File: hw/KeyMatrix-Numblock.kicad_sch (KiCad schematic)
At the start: 62 parts, among them SW2300 SW_Cherry_MX_RGB, SW2301 SW_Cherry_MX_RGB, SW2302 SW_Cherry_MX_RGB, SW2303 SW_Cherry_MX_RGB, SW2304 SW_Cherry_MX_RGB, SW2305 SW_Cherry_MX_RGB, SW2306 SW_Cherry_MX_RGB, SW2307 SW_Cherry_MX_RGB, SW2308 SW_Cherry_MX_RGB, SW2309 SW_Cherry_MX_RGB, SW2310 SW_Cherry_MX_RGB, SW2311 SW_Cherry_MX_RGB, SW2312 SW_Cherry_MX_RGB, SW2313 SW_Cherry_MX_RGB, SW2314 SW_Cherry_MX_RGB, SW2315 SW_Cherry_MX_RGB, SW2316 SW_Cherry_MX_RGB, SW2317 SW_Cherry_MX_RGB, X2300 STAB-0G990224, X2301 STAB-0G990224, X2302 STAB-0G990224, X2303 Keycap-R1-1x1, X2304 Keycap-R1-1x1, X2305 Keycap-R1-1x1, X2306 Keycap-R1-1x1, X2307 Keycap-R1-1x1, X2308 Keycap-R1-1x1, X2309 Keycap-R1-1x1, X2310 Keycap-R1-1x1, X2311 Keycap-R1-2x1, X2312 Keycap-R1-1x1, X2313 Keycap-R1-1x1, X2314 Keycap-R1-1x1, X2315 Keycap-R1-1x1, X2316 Keycap-R1-1x1, X2317 Keycap-R1-1x1, X2318 Keycap-R1-2x1, X2319 Keycap-R1-2x1, X2320 Keycap-R1-1x1

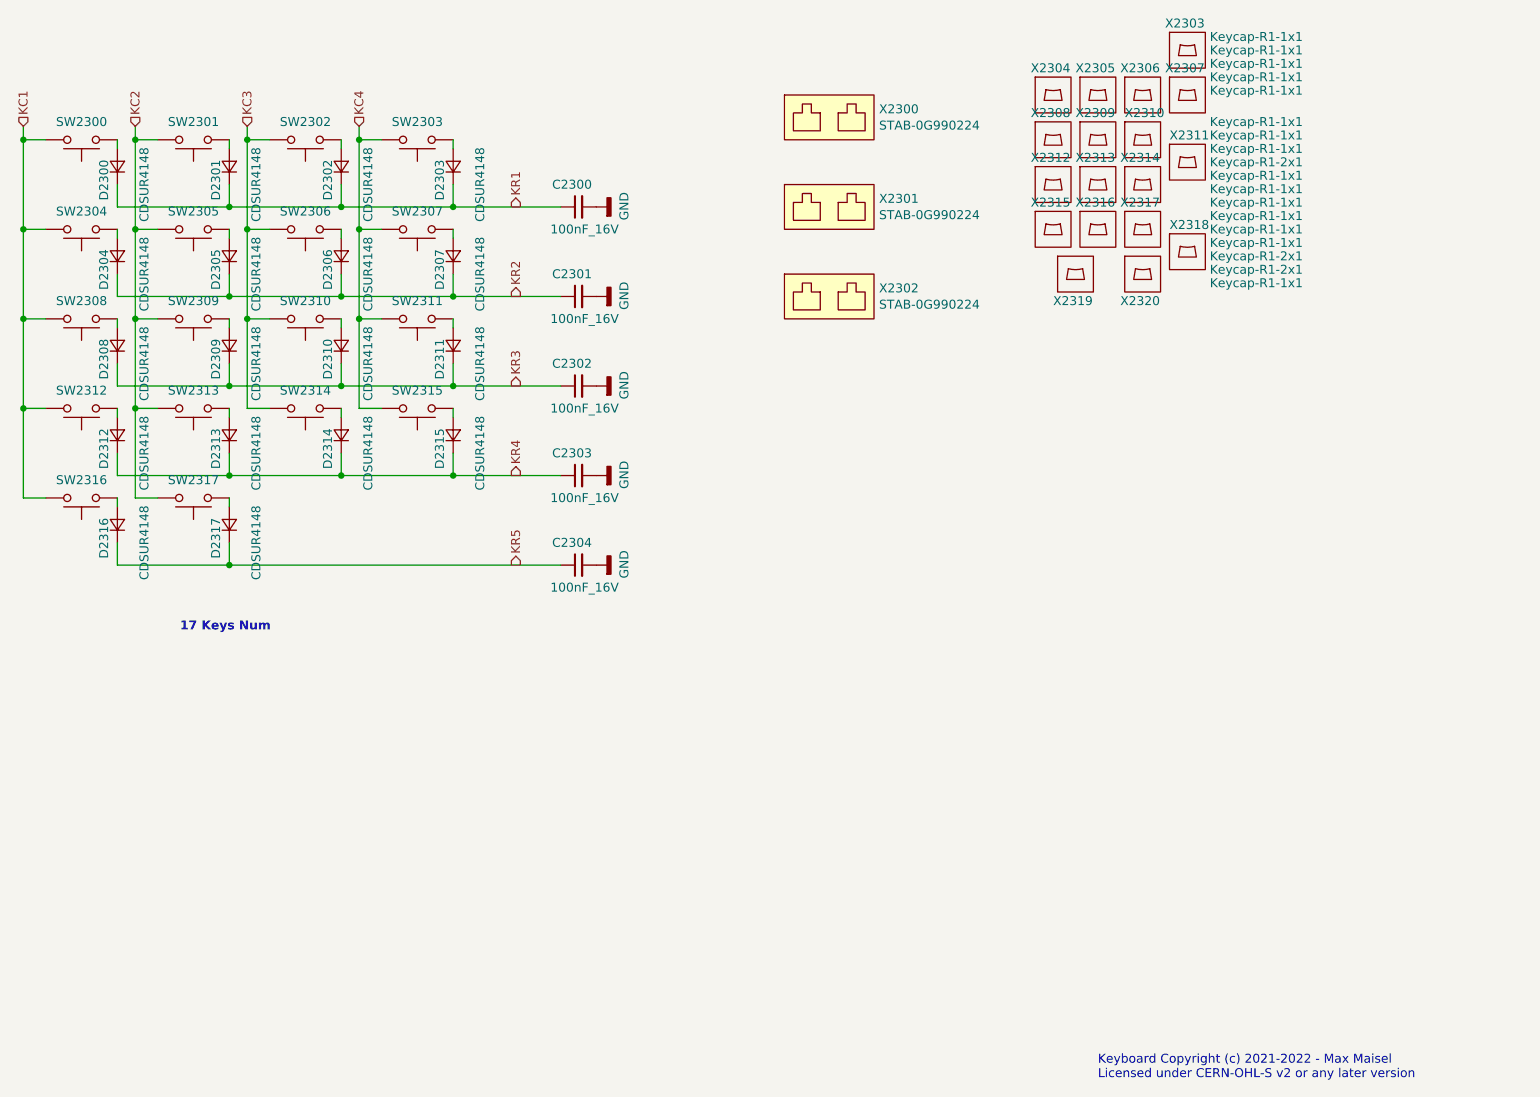
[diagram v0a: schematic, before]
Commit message: Add ESD diodes to key matrix pins.
Better save than sorry.
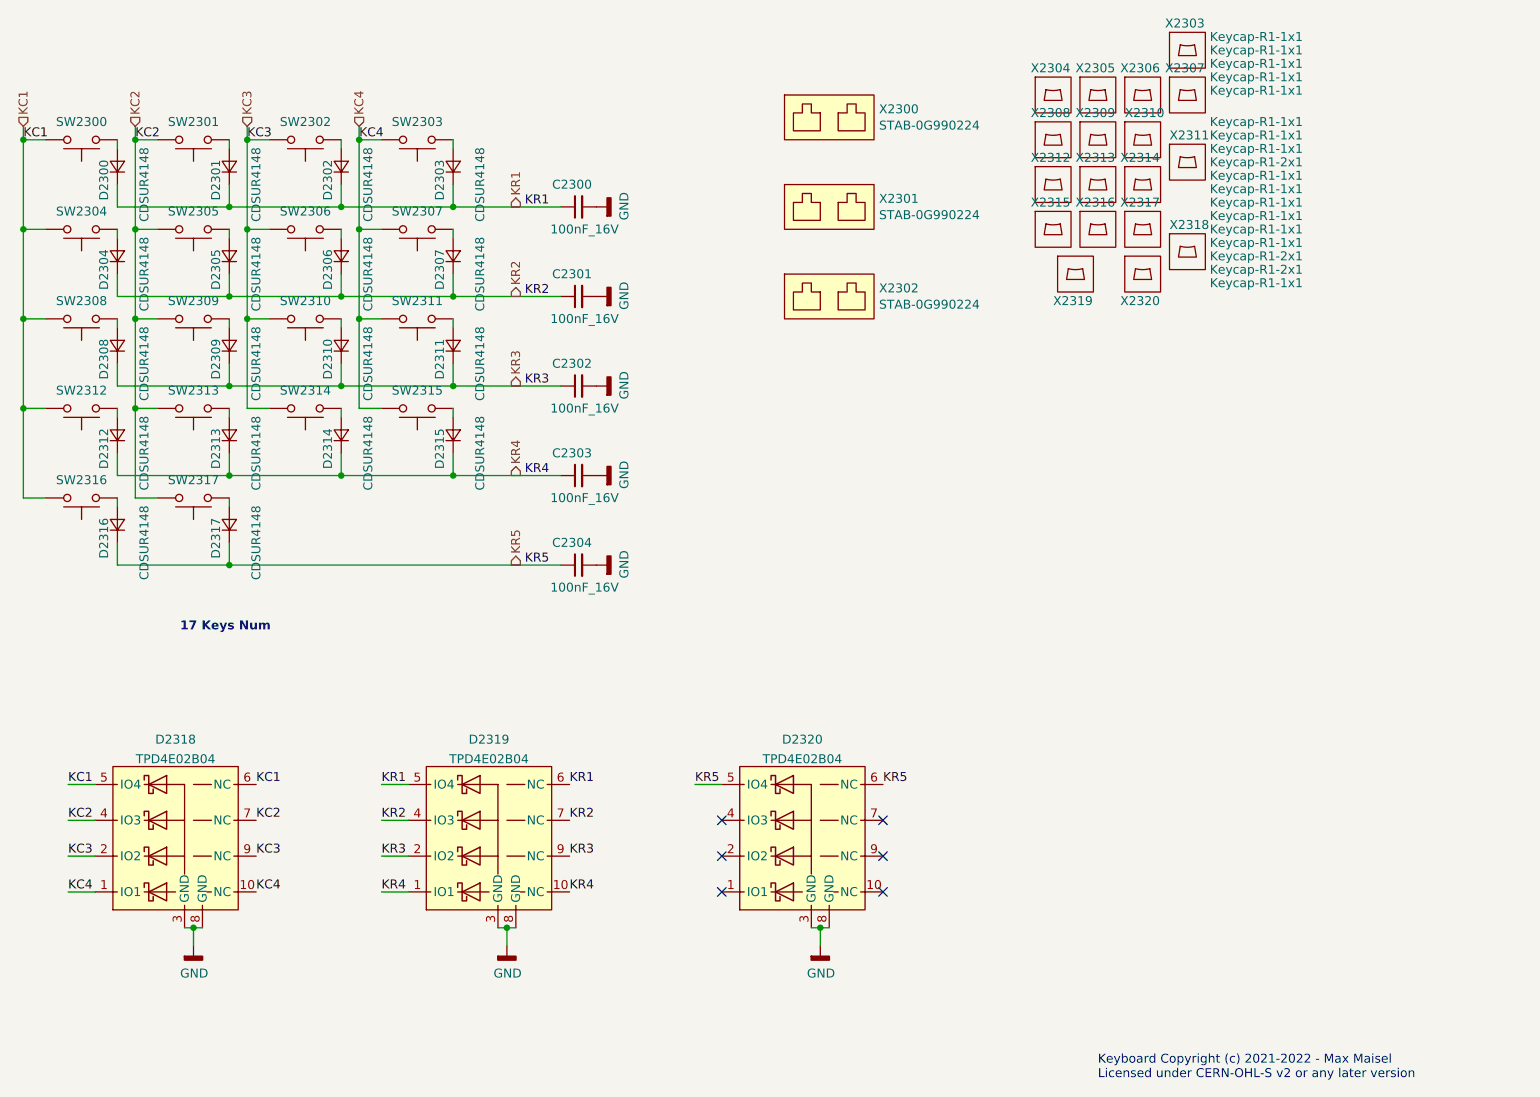
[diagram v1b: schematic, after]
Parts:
- added D2318, D2319, D2320: TPD4E02B04, Keyboard:USON10, symbol Keyboard:TPD4E02B04
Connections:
- net GND: now also D2318.3 (GND), D2318.8 (GND), D2319.3 (GND), D2319.8 (GND), D2320.3 (GND), D2320.8 (GND)
- net KC1: now also D2318.5 (IO4), D2318.6 (NC)
- net KC2: now also D2318.4 (IO3), D2318.7 (NC)
- net KC3: now also D2318.2 (IO2), D2318.9 (NC)
- net KC4: now also D2318.1 (IO1), D2318.10 (NC)
- net KR1: now also D2319.5 (IO4), D2319.6 (NC)
- net KR2: now also D2319.4 (IO3), D2319.7 (NC)
- net KR3: now also D2319.2 (IO2), D2319.9 (NC)
- net KR4: now also D2319.1 (IO1), D2319.10 (NC)
- net KR5: now also D2320.5 (IO4), D2320.6 (NC)
- no-connect marks 0 -> 6

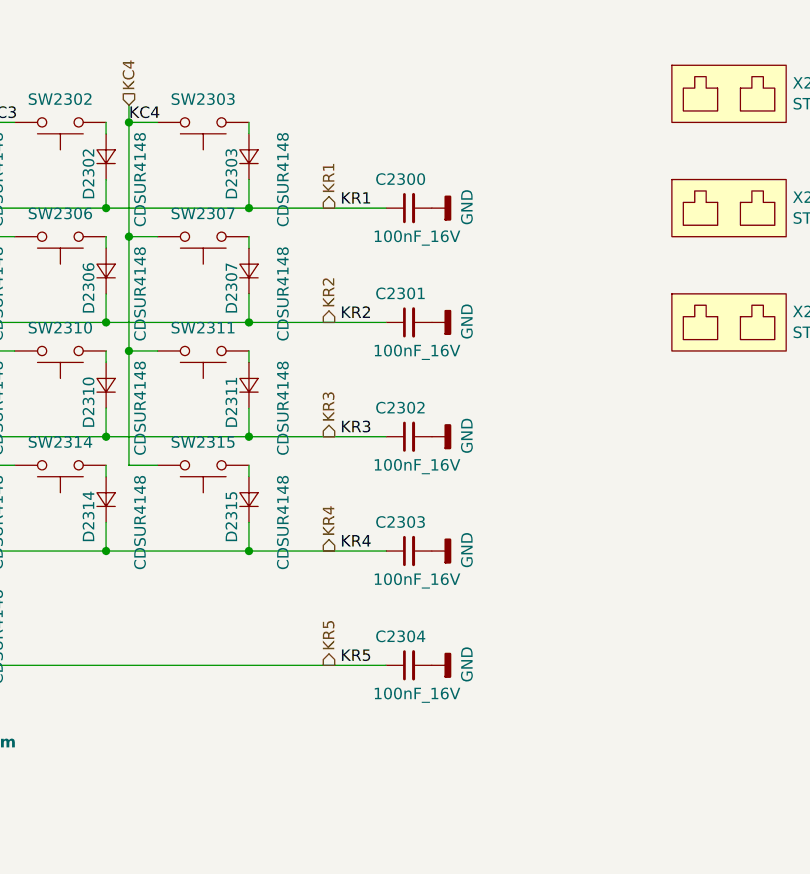
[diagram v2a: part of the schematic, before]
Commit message: Change key matrix capacitors to 220pF.
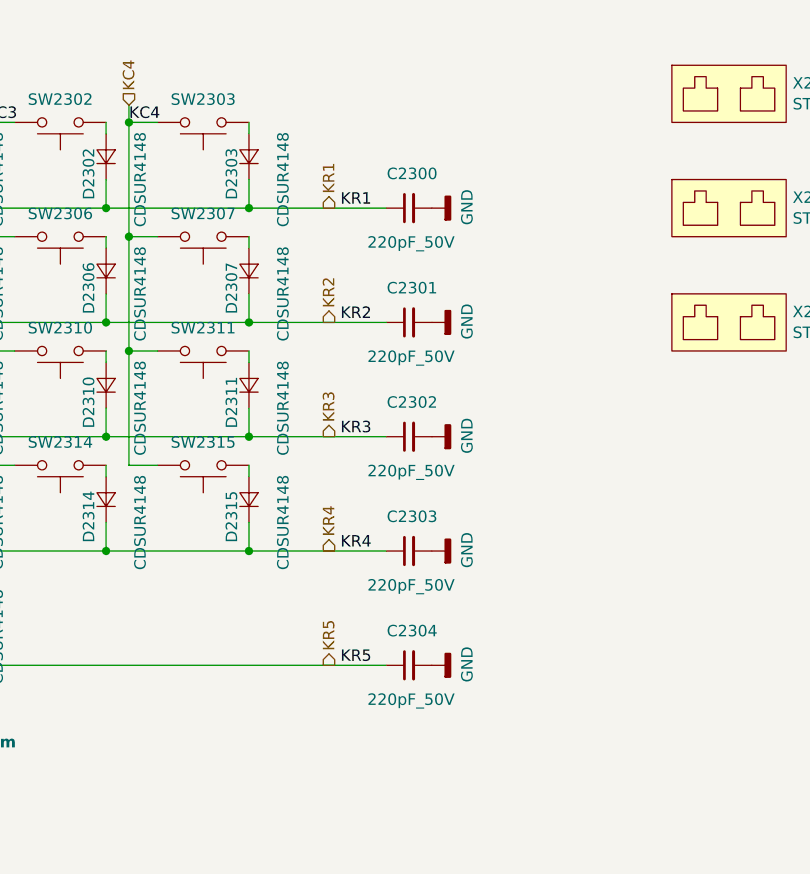
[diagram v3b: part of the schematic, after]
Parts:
- removed C2300, C2301, C2302, C2303, C2304: 100nF_16V, Keyboard:C_0402, symbol Keyboard:100nF_16V
- added C2300, C2301, C2302, C2303, C2304: 220pF_50V, Keyboard:C_0402, symbol Keyboard:220pF_50V
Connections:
- net GND: now also C2300.2, C2301.2, C2302.2, C2303.2, C2304.2
- net KR1: now also C2300.1
- net KR2: now also C2301.1
- net KR3: now also C2302.1
- net KR4: now also C2303.1
- net KR5: now also C2304.1
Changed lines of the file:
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@@
-    (pin "2")
-  )
-  (symbol (lib_id "Keyboard:100nF_16V") (at 104.14 47.625 90) (unit 1)
-    (in_bom yes) (on_board yes)
-    (property "Reference" "C2300" (id 0) (at 106.045 44.45 90)
-      (effects (font (size 1.27 1.27)) (justify left))
-    )
-    (property "Value" "100nF_16V" (id 1) (at 109.855 50.8 90)
-      (effects (font (size 1.27 1.27)) (justify left))
-    )
-    (property "Footprint" "Keyboard:C_0402" (id 2) (at 104.902 49.911 0)
-      (effects (font (size 1.27 1.27)) hide)
-    )
-    (property "Datasheet" "80-C0402C104K4R" (id 3) (at 102.362 47.371 0)
-      (effects (font (size 1.27 1.27)) hide)
-    )
-    (property "mouser#" "80-C0402C104K4R" (id 4) (at 99.822 44.831 0)
-      (effects (font (size 1.524 1.524)) hide)
-    )
-    (pin "1")
     (pin "2")
   )
@@
     (pin "1")
   )
-  (symbol (lib_id "Keyboard:100nF_16V") (at 104.14 73.025 90) (unit 1)
-    (in_bom yes) (on_board yes)
-    (property "Reference" "C2302" (id 0) (at 106.045 69.85 90)
-      (effects (font (size 1.27 1.27)) (justify left))
-    )
-    (property "Value" "100nF_16V" (id 1) (at 109.855 76.2 90)
-      (effects (font (size 1.27 1.27)) (justify left))
-    )
-    (property "Footprint" "Keyboard:C_0402" (id 2) (at 104.902 75.311 0)
-      (effects (font (size 1.27 1.27)) hide)
-    )
-    (property "Datasheet" "80-C0402C104K4R" (id 3) (at 102.362 72.771 0)
-      (effects (font (size 1.27 1.27)) hide)
-    )
-    (property "mouser#" "80-C0402C104K4R" (id 4) (at 99.822 70.231 0)
-      (effects (font (size 1.524 1.524)) hide)
-    )
-    (pin "1")
-    (pin "2")
-  )
   (symbol (lib_id "Keyboard:GND") (at 106.68 73.025 90) (unit 1)
     (in_bom yes) (on_board yes)
@@
     (pin "1")
   )
-  (symbol (lib_id "Keyboard:100nF_16V") (at 104.14 85.725 90) (unit 1)
-    (in_bom yes) (on_board yes)
-    (property "Reference" "C2303" (id 0) (at 106.045 82.55 90)
-      (effects (font (size 1.27 1.27)) (justify left))
-    )
-    (property "Value" "100nF_16V" (id 1) (at 109.855 88.9 90)
-      (effects (font (size 1.27 1.27)) (justify left))
-    )
-    (property "Footprint" "Keyboard:C_0402" (id 2) (at 104.902 88.011 0)
-      (effects (font (size 1.27 1.27)) hide)
-    )
-    (property "Datasheet" "80-C0402C104K4R" (id 3) (at 102.362 85.471 0)
-      (effects (font (size 1.27 1.27)) hide)
-    )
-    (property "mouser#" "80-C0402C104K4R" (id 4) (at 99.822 82.931 0)
-      (effects (font (size 1.524 1.524)) hide)
-    )
-    (pin "1")
-    (pin "2")
-  )
   (symbol (lib_id "Keyboard:GND") (at 106.68 85.725 90) (unit 1)
     (in_bom yes) (on_board yes)
@@
     (pin "1")
   )
-  (symbol (lib_id "Keyboard:100nF_16V") (at 104.14 98.425 90) (unit 1)
-    (in_bom yes) (on_board yes)
-    (property "Reference" "C2304" (id 0) (at 106.045 95.25 90)
-      (effects (font (size 1.27 1.27)) (justify left))
-    )
-    (property "Value" "100nF_16V" (id 1) (at 109.855 101.6 90)
-      (effects (font (size 1.27 1.27)) (justify left))
-    )
-    (property "Footprint" "Keyboard:C_0402" (id 2) (at 104.902 100.711 0)
-      (effects (font (size 1.27 1.27)) hide)
-    )
-    (property "Datasheet" "80-C0402C104K4R" (id 3) (at 102.362 98.171 0)
-      (effects (font (size 1.27 1.27)) hide)
-    )
-    (property "mouser#" "80-C0402C104K4R" (id 4) (at 99.822 95.631 0)
-      (effects (font (size 1.524 1.524)) hide)
-    )
-    (pin "1")
-    (pin "2")
-  )
   (symbol (lib_id "Keyboard:GND") (at 106.68 98.425 90) (unit 1)
     (in_bom yes) (on_board yes)
@@
     (property "reichelt#" "CHERRY MX1A-G1NA" (id 4) (at 81.28 76.2 0)
       (effects (font (size 1.27 1.27)) hide)
-    )
-    (pin "1")
-    (pin "2")
-  )
-  (symbol (lib_id "Keyboard:100nF_16V") (at 104.14 60.325 90) (unit 1)
-    (in_bom yes) (on_board yes)
-    (property "Reference" "C2301" (id 0) (at 106.045 57.15 90)
-      (effects (font (size 1.27 1.27)) (justify left))
-    )
-    (property "Value" "100nF_16V" (id 1) (at 109.855 63.5 90)
-      (effects (font (size 1.27 1.27)) (justify left))
-    )
-    (property "Footprint" "Keyboard:C_0402" (id 2) (at 104.902 62.611 0)
-      (effects (font (size 1.27 1.27)) hide)
-    )
-    (property "Datasheet" "80-C0402C104K4R" (id 3) (at 102.362 60.071 0)
-      (effects (font (size 1.27 1.27)) hide)
-    )
-    (property "mouser#" "80-C0402C104K4R" (id 4) (at 99.822 57.531 0)
-      (effects (font (size 1.524 1.524)) hide)
     )
     (pin "1")
@@
     )
     (pin "1")
+  )
+  (symbol (lib_id "Keyboard:220pF_50V") (at 104.14 47.625 90) (unit 1)
+    (in_bom yes) (on_board yes)
+    (property "Reference" "C2300" (id 0) (at 107.315 43.815 90)
+      (effects (font (size 1.27 1.27)) (justify left))
+    )
+    (property "Value" "220pF_50V" (id 1) (at 109.22 51.435 90)
+      (effects (font (size 1.27 1.27)) (justify left))
+    )
+    (property "Footprint" "Keyboard:C_0402" (id 2) (at 104.902 49.911 0)
+      (effects (font (size 1.27 1.27)) hide)
+    )
+    (property "Datasheet" "https://www.mouser.de/datasheet/2/281/1/GRM0335C1H221JA01_01A-1980773.pdf" (id 3) (at 102.362 47.371 0)
+      (effects (font (size 1.27 1.27)) hide)
+    )
+    (property "mouser#" "81-GRM0335C1H221JA1D" (id 4) (at 99.822 44.831 0)
+      (effects (font (size 1.524 1.524)) hide)
+    )
+    (property "manf#" "GRM0335C1H221JA01D" (id 5) (at 104.14 47.625 0)
+      (effects (font (size 1.27 1.27)) hide)
+    )
+    (pin "1")
+    (pin "2")
   )
   (symbol (lib_id "Keyboard:TPD4E02B04") (at 135.89 137.16 0) (unit 1)
@@
     (pin "9")
   )
+  (symbol (lib_id "Keyboard:220pF_50V") (at 104.14 73.025 90) (unit 1)
+    (in_bom yes) (on_board yes)
+    (property "Reference" "C2302" (id 0) (at 107.315 69.215 90)
+      (effects (font (size 1.27 1.27)) (justify left))
+    )
+    (property "Value" "220pF_50V" (id 1) (at 109.22 76.835 90)
+      (effects (font (size 1.27 1.27)) (justify left))
+    )
+    (property "Footprint" "Keyboard:C_0402" (id 2) (at 104.902 75.311 0)
+      (effects (font (size 1.27 1.27)) hide)
+    )
+    (property "Datasheet" "https://www.mouser.de/datasheet/2/281/1/GRM0335C1H221JA01_01A-1980773.pdf" (id 3) (at 102.362 72.771 0)
+      (effects (font (size 1.27 1.27)) hide)
+    )
+    (property "mouser#" "81-GRM0335C1H221JA1D" (id 4) (at 99.822 70.231 0)
+      (effects (font (size 1.524 1.524)) hide)
+    )
+    (property "manf#" "GRM0335C1H221JA01D" (id 5) (at 104.14 73.025 0)
+      (effects (font (size 1.27 1.27)) hide)
+    )
+    (pin "1")
+    (pin "2")
+  )
+  (symbol (lib_id "Keyboard:220pF_50V") (at 104.14 98.425 90) (unit 1)
+    (in_bom yes) (on_board yes)
+    (property "Reference" "C2304" (id 0) (at 107.315 94.615 90)
+      (effects (font (size 1.27 1.27)) (justify left))
+    )
+    (property "Value" "220pF_50V" (id 1) (at 109.22 102.235 90)
+      (effects (font (size 1.27 1.27)) (justify left))
+    )
+    (property "Footprint" "Keyboard:C_0402" (id 2) (at 104.902 100.711 0)
+      (effects (font (size 1.27 1.27)) hide)
+    )
+    (property "Datasheet" "https://www.mouser.de/datasheet/2/281/1/GRM0335C1H221JA01_01A-1980773.pdf" (id 3) (at 102.362 98.171 0)
+      (effects (font (size 1.27 1.27)) hide)
+    )
+    (property "mouser#" "81-GRM0335C1H221JA1D" (id 4) (at 99.822 95.631 0)
+      (effects (font (size 1.524 1.524)) hide)
+    )
+    (property "manf#" "GRM0335C1H221JA01D" (id 5) (at 104.14 98.425 0)
+      (effects (font (size 1.27 1.27)) hide)
+    )
+    (pin "1")
+    (pin "2")
+  )
+  (symbol (lib_id "Keyboard:220pF_50V") (at 104.14 85.725 90) (unit 1)
+    (in_bom yes) (on_board yes)
+    (property "Reference" "C2303" (id 0) (at 107.315 81.915 90)
+      (effects (font (size 1.27 1.27)) (justify left))
+    )
+    (property "Value" "220pF_50V" (id 1) (at 109.22 89.535 90)
+      (effects (font (size 1.27 1.27)) (justify left))
+    )
+    (property "Footprint" "Keyboard:C_0402" (id 2) (at 104.902 88.011 0)
+      (effects (font (size 1.27 1.27)) hide)
+    )
+    (property "Datasheet" "https://www.mouser.de/datasheet/2/281/1/GRM0335C1H221JA01_01A-1980773.pdf" (id 3) (at 102.362 85.471 0)
+      (effects (font (size 1.27 1.27)) hide)
+    )
+    (property "mouser#" "81-GRM0335C1H221JA1D" (id 4) (at 99.822 82.931 0)
+      (effects (font (size 1.524 1.524)) hide)
+    )
+    (property "manf#" "GRM0335C1H221JA01D" (id 5) (at 104.14 85.725 0)
+      (effects (font (size 1.27 1.27)) hide)
+    )
+    (pin "1")
+    (pin "2")
+  )
+  (symbol (lib_id "Keyboard:220pF_50V") (at 104.14 60.325 90) (unit 1)
+    (in_bom yes) (on_board yes)
+    (property "Reference" "C2301" (id 0) (at 107.315 56.515 90)
+      (effects (font (size 1.27 1.27)) (justify left))
+    )
+    (property "Value" "220pF_50V" (id 1) (at 109.22 64.135 90)
+      (effects (font (size 1.27 1.27)) (justify left))
+    )
+    (property "Footprint" "Keyboard:C_0402" (id 2) (at 104.902 62.611 0)
+      (effects (font (size 1.27 1.27)) hide)
+    )
+    (property "Datasheet" "https://www.mouser.de/datasheet/2/281/1/GRM0335C1H221JA01_01A-1980773.pdf" (id 3) (at 102.362 60.071 0)
+      (effects (font (size 1.27 1.27)) hide)
+    )
+    (property "mouser#" "81-GRM0335C1H221JA1D" (id 4) (at 99.822 57.531 0)
+      (effects (font (size 1.524 1.524)) hide)
+    )
+    (property "manf#" "GRM0335C1H221JA01D" (id 5) (at 104.14 60.325 0)
+      (effects (font (size 1.27 1.27)) hide)
+    )
+    (pin "1")
+    (pin "2")
+  )
   (symbol (lib_id "Keyboard:GND") (at 138.43 152.4 0) (unit 1)
